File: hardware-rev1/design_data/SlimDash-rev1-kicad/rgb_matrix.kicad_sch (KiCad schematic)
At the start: 35 parts

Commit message: trace routing progress
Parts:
- added JP1: SolderJumper_2_Open, Jumper:SolderJumper-2_P1.3mm_Open_RoundedPad1.0x1.5mm, symbol Jumper:SolderJumper_2_Open
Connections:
- net DIN: now also JP1.1 (A); no longer LED35.3 (DIN)
- new net: JP1.2 (B), LED35.3 (DIN)
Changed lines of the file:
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@@
-	(wire
-		(pts
-			(xy 30.48 34.29) (xy 38.1 34.29)
-		)
-		(stroke
-			(width 0)
-			(type default)
-		)
-	)
 	(wire
 		(pts
@@
 					(unit 1)
 				)
+			)
+		)
+	)
+	(symbol
+		(lib_id "Jumper:SolderJumper_2_Open")
+		(at 34.29 34.29 0)
+		(unit 1)
+		(exclude_from_sim yes)
+		(in_bom no)
+		(on_board yes)
+		(dnp no)
+		(property "Reference" "JP1"
+			(at 28.448 35.56 0)
+			(effects
+				(font
+					(size 1.27 1.27)
+				)
+			)
+		)
+		(property "Value" "SolderJumper_2_Open"
+			(at 28.448 38.1 0)
+			(effects
+				(font
+					(size 1.27 1.27)
+				)
+			)
+		)
+		(property "Footprint" "Jumper:SolderJumper-2_P1.3mm_Open_RoundedPad1.0x1.5mm"
+			(at 34.29 34.29 0)
+			(effects
+				(font
+					(size 1.27 1.27)
+				)
+				(hide yes)
+			)
+		)
+		(property "Datasheet" "~"
+			(at 34.29 34.29 0)
+			(effects
+				(font
+					(size 1.27 1.27)
+				)
+				(hide yes)
+			)
+		)
+		(property "Description" "Solder Jumper, 2-pole, open"
+			(at 34.29 34.29 0)
+			(effects
+				(font
+					(size 1.27 1.27)
+				)
+				(hide yes)
+			)
+		)
+		(pin "2"
+		)
+		(pin "1"
+		)
+		(instances
+			(project ""
+				(path "/d2049868-8659-40e1-9f69-d91a53267064/01f902d0-715d-4e61-9332-0e6e120b87e0"
+					(reference "JP1")
+					(unit 1)
+				)

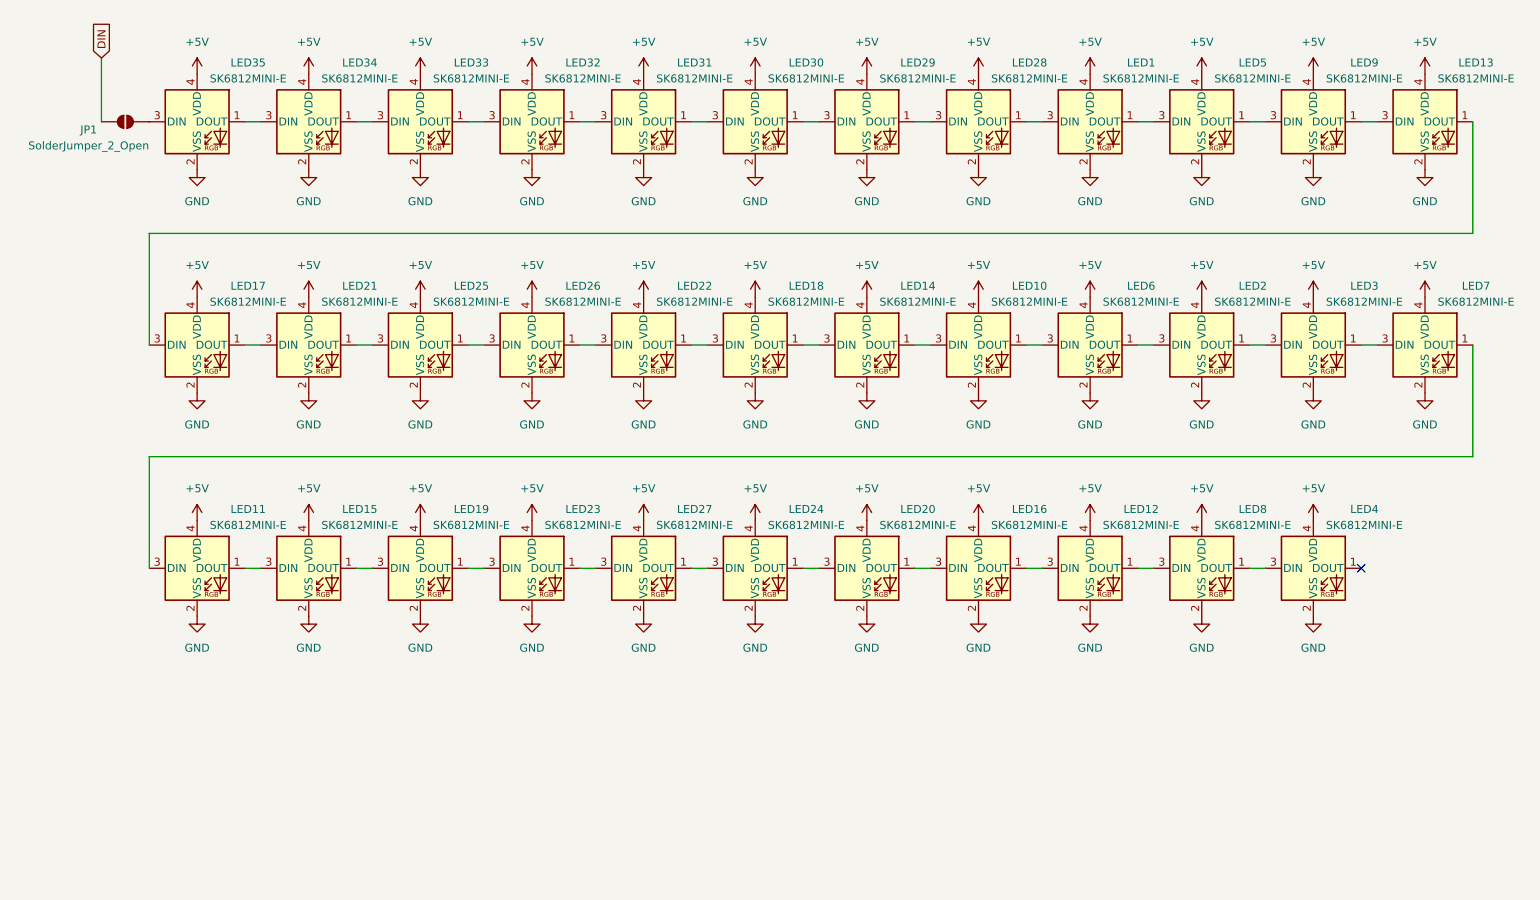
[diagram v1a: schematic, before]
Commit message: more routing and fixing footprints
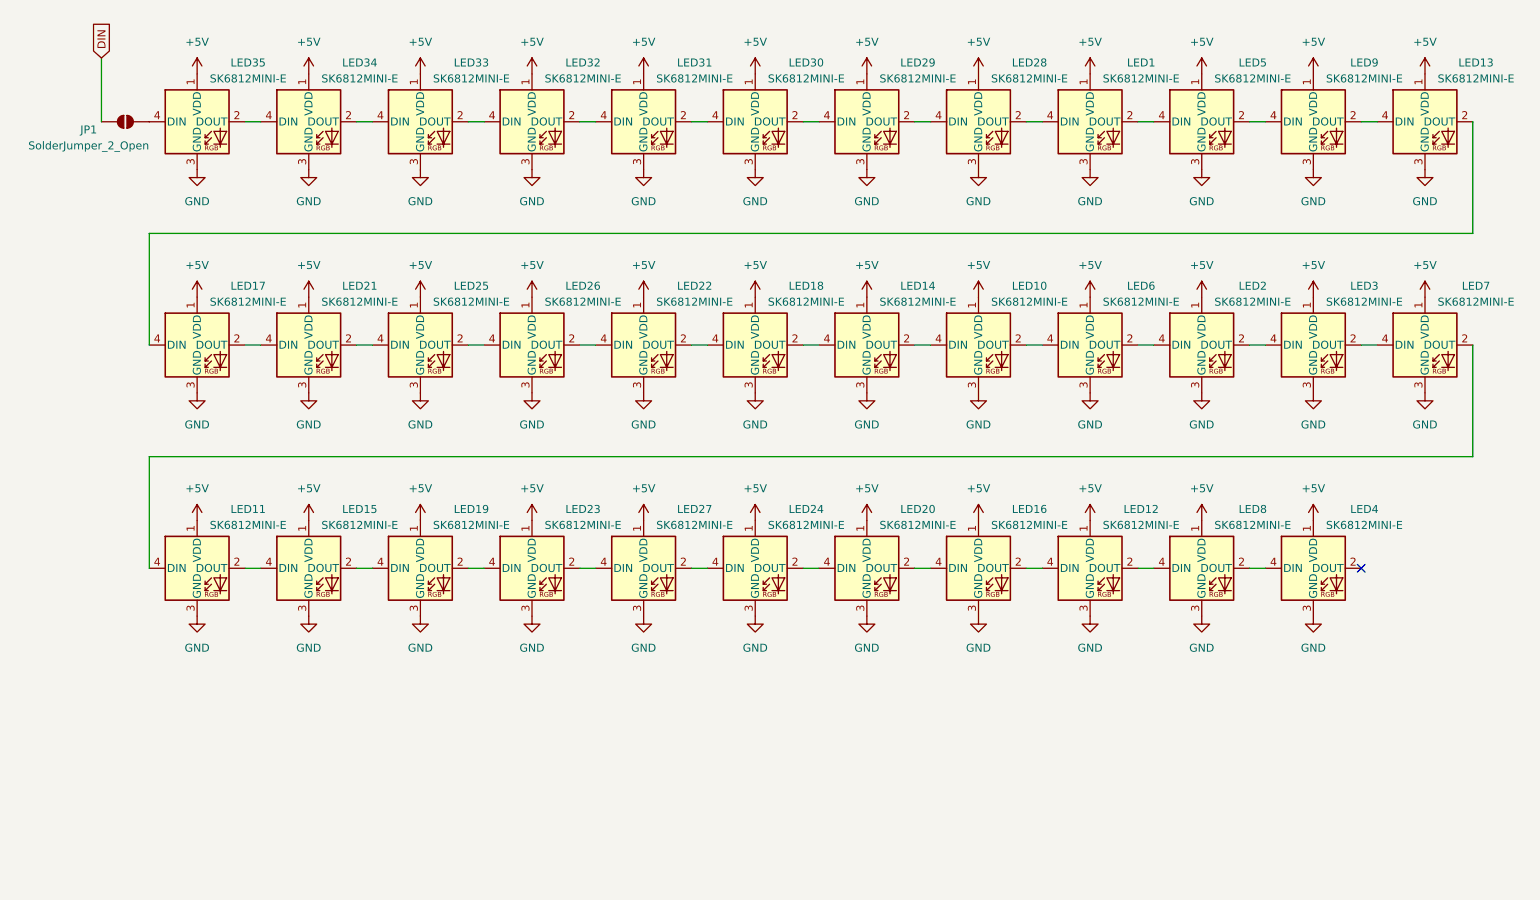
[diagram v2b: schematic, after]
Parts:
- LED1, LED10, LED11, LED12, LED13, LED14, LED15, LED16, LED17, LED18, LED19, LED2, LED20, LED21, LED22, LED23, LED24, LED25, LED26, LED27, LED28, LED29, LED3, LED30, LED31, LED32, LED33, LED34, LED35, LED4, LED5, LED6, LED7, LED8, LED9: symbol LED:SK6812MINI -> mzm_kicad:SK6812MINI-E
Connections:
- net +5V: now also LED1.1 (VDD), LED10.1 (VDD), LED11.1 (VDD), LED12.1 (VDD), LED13.1 (VDD), LED14.1 (VDD), LED15.1 (VDD), LED16.1 (VDD), LED17.1 (VDD), LED18.1 (VDD), LED19.1 (VDD), LED2.1 (VDD), LED20.1 (VDD), LED21.1 (VDD), LED22.1 (VDD), LED23.1 (VDD), LED24.1 (VDD), LED25.1 (VDD), LED26.1 (VDD), LED27.1 (VDD), LED28.1 (VDD), LED29.1 (VDD), LED3.1 (VDD), LED30.1 (VDD), LED31.1 (VDD), LED32.1 (VDD), LED33.1 (VDD), LED34.1 (VDD), LED35.1 (VDD), LED4.1 (VDD), LED5.1 (VDD), LED6.1 (VDD), LED7.1 (VDD), LED8.1 (VDD), LED9.1 (VDD); no longer LED1.4 (VDD), LED10.4 (VDD), LED11.4 (VDD), LED12.4 (VDD), LED13.4 (VDD), LED14.4 (VDD), LED15.4 (VDD), LED16.4 (VDD), LED17.4 (VDD), LED18.4 (VDD), LED19.4 (VDD), LED2.4 (VDD), LED20.4 (VDD), LED21.4 (VDD), LED22.4 (VDD), LED23.4 (VDD), LED24.4 (VDD), LED25.4 (VDD), LED26.4 (VDD), LED27.4 (VDD), LED28.4 (VDD), LED29.4 (VDD), LED3.4 (VDD), LED30.4 (VDD), LED31.4 (VDD), LED32.4 (VDD), LED33.4 (VDD), LED34.4 (VDD), LED35.4 (VDD), LED4.4 (VDD), LED5.4 (VDD), LED6.4 (VDD), LED7.4 (VDD), LED8.4 (VDD), LED9.4 (VDD)
- net GND: now also LED1.3 (GND), LED10.3 (GND), LED11.3 (GND), LED12.3 (GND), LED13.3 (GND), LED14.3 (GND), LED15.3 (GND), LED16.3 (GND), LED17.3 (GND), LED18.3 (GND), LED19.3 (GND), LED2.3 (GND), LED20.3 (GND), LED21.3 (GND), LED22.3 (GND), LED23.3 (GND), LED24.3 (GND), LED25.3 (GND), LED26.3 (GND), LED27.3 (GND), LED28.3 (GND), LED29.3 (GND), LED3.3 (GND), LED30.3 (GND), LED31.3 (GND), LED32.3 (GND), LED33.3 (GND), LED34.3 (GND), LED35.3 (GND), LED4.3 (GND), LED5.3 (GND), LED6.3 (GND), LED7.3 (GND), LED8.3 (GND), LED9.3 (GND); no longer LED1.2 (VSS), LED10.2 (VSS), LED11.2 (VSS), LED12.2 (VSS), LED13.2 (VSS), LED14.2 (VSS), LED15.2 (VSS), LED16.2 (VSS), LED17.2 (VSS), LED18.2 (VSS), LED19.2 (VSS), LED2.2 (VSS), LED20.2 (VSS), LED21.2 (VSS), LED22.2 (VSS), LED23.2 (VSS), LED24.2 (VSS), LED25.2 (VSS), LED26.2 (VSS), LED27.2 (VSS), LED28.2 (VSS), LED29.2 (VSS), LED3.2 (VSS), LED30.2 (VSS), LED31.2 (VSS), LED32.2 (VSS), LED33.2 (VSS), LED34.2 (VSS), LED35.2 (VSS), LED4.2 (VSS), LED5.2 (VSS), LED6.2 (VSS), LED7.2 (VSS), LED8.2 (VSS), LED9.2 (VSS)
- net at JP1.2 (B): now also LED35.4 (DIN); no longer LED35.3 (DIN)
- new net: LED11.4 (DIN), LED7.2 (DOUT)
- new net: LED3.2 (DOUT), LED7.4 (DIN)
- new net: LED16.4 (DIN), LED20.2 (DOUT)
- new net: LED20.4 (DIN), LED24.2 (DOUT)
- new net: LED32.4 (DIN), LED33.2 (DOUT)
- new net: LED33.4 (DIN), LED34.2 (DOUT)
- new net: LED2.2 (DOUT), LED3.4 (DIN)
- new net: LED2.4 (DIN), LED6.2 (DOUT)
- new net: LED12.2 (DOUT), LED8.4 (DIN)
- new net: LED12.4 (DIN), LED16.2 (DOUT)
- new net: LED21.2 (DOUT), LED25.4 (DIN)
- new net: LED17.2 (DOUT), LED21.4 (DIN)
- new net: LED25.2 (DOUT), LED26.4 (DIN)
- new net: LED11.2 (DOUT), LED15.4 (DIN)
- new net: LED1.2 (DOUT), LED5.4 (DIN)
- new net: LED1.4 (DIN), LED28.2 (DOUT)
- new net: LED15.2 (DOUT), LED19.4 (DIN)
- new net: LED13.4 (DIN), LED9.2 (DOUT)
- new net: LED5.2 (DOUT), LED9.4 (DIN)
- new net: LED28.4 (DIN), LED29.2 (DOUT)
- new net: LED10.2 (DOUT), LED6.4 (DIN)
- new net: LED13.2 (DOUT), LED17.4 (DIN)
- new net: LED29.4 (DIN), LED30.2 (DOUT)
- new net: LED30.4 (DIN), LED31.2 (DOUT)
- new net: LED34.4 (DIN), LED35.2 (DOUT)
- new net: LED18.4 (DIN), LED22.2 (DOUT)
- new net: LED22.4 (DIN), LED26.2 (DOUT)
- new net: LED23.2 (DOUT), LED27.4 (DIN)
- new net: LED19.2 (DOUT), LED23.4 (DIN)
- new net: LED10.4 (DIN), LED14.2 (DOUT)
- new net: LED14.4 (DIN), LED18.2 (DOUT)
- new net: LED4.4 (DIN), LED8.2 (DOUT)
- new net: LED31.4 (DIN), LED32.2 (DOUT)
- new net: LED24.4 (DIN), LED27.2 (DOUT)

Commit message: finalize pcb layout
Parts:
- added U5: SN74LVC1T45DRL, mzm_LCSC:SOT-563_SN74LVC1T45DRLR, symbol Logic_LevelTranslator:SN74LVC1T45DRL
- LED1, LED10, LED11, LED12, LED13, LED14, LED15, LED16, LED17, LED18, LED19, LED2, LED20, LED21, LED22, LED23, LED24, LED25, LED26, LED27, LED28, LED29, LED3, LED30, LED31, LED32, LED33, LED34, LED35, LED4, LED5, LED6, LED7, LED8, LED9: LCSC (none) -> C5149201
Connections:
- net +5V: now also U5.1 (VCCA)
- net DIN: now also U5.4 (B); no longer JP1.1 (A)
- net GND: now also U5.2 (GND), U5.5 (DIR)
- new net: JP1.1 (A), U5.3 (A)
- new net +3V3: U5.6 (VCCB)
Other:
- moved on the sheet: JP1, LED1, LED10, LED11, LED12, LED13, LED14, LED15, LED16, LED17, LED18, LED19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
